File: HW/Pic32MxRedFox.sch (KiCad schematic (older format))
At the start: 40 parts, among them J1 USB_C_Receptacle_USB2.0, J2 Conn_02x05_Odd_Even, J3 Conn_01x20, J4 Conn_01x20, SW1 SW_Push, SW2 SW_Push, U1 LD1117S33TR_SOT223, U2 LN1134A332MR-G, U3 SRV05-4, U4 PIC32MX270F256D-IPT, Y1 Crystal_GND2, Y2 Crystal

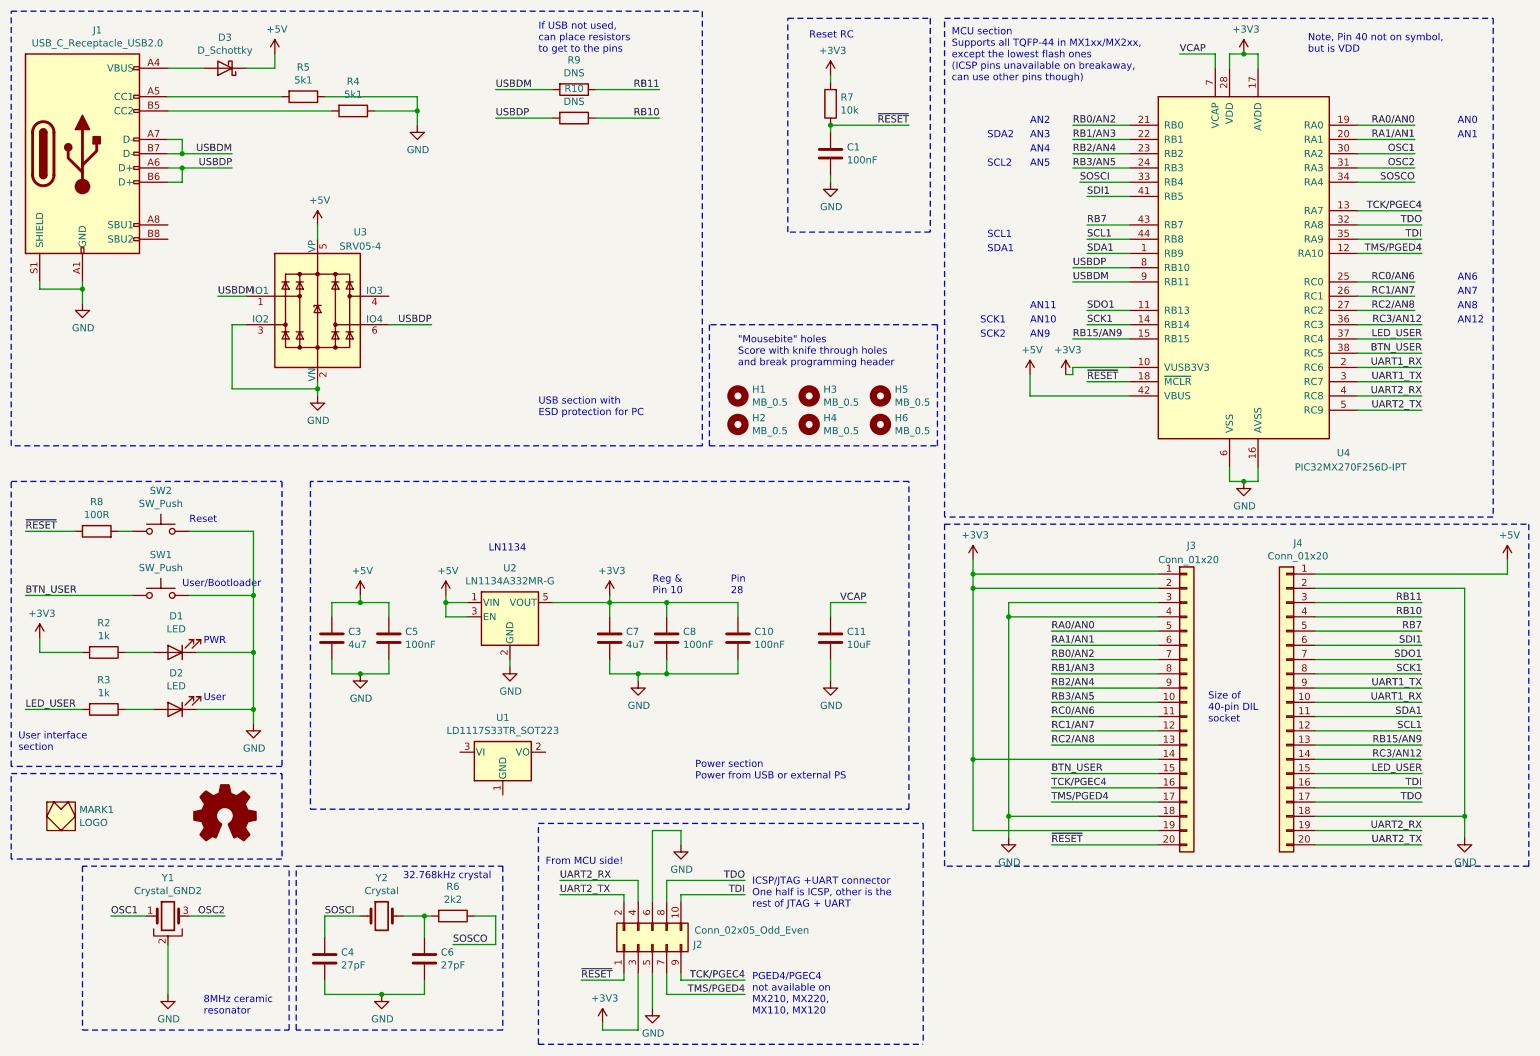
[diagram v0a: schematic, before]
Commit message: New revision that actually fits in a DIP40 socket. Pinout stays the same.
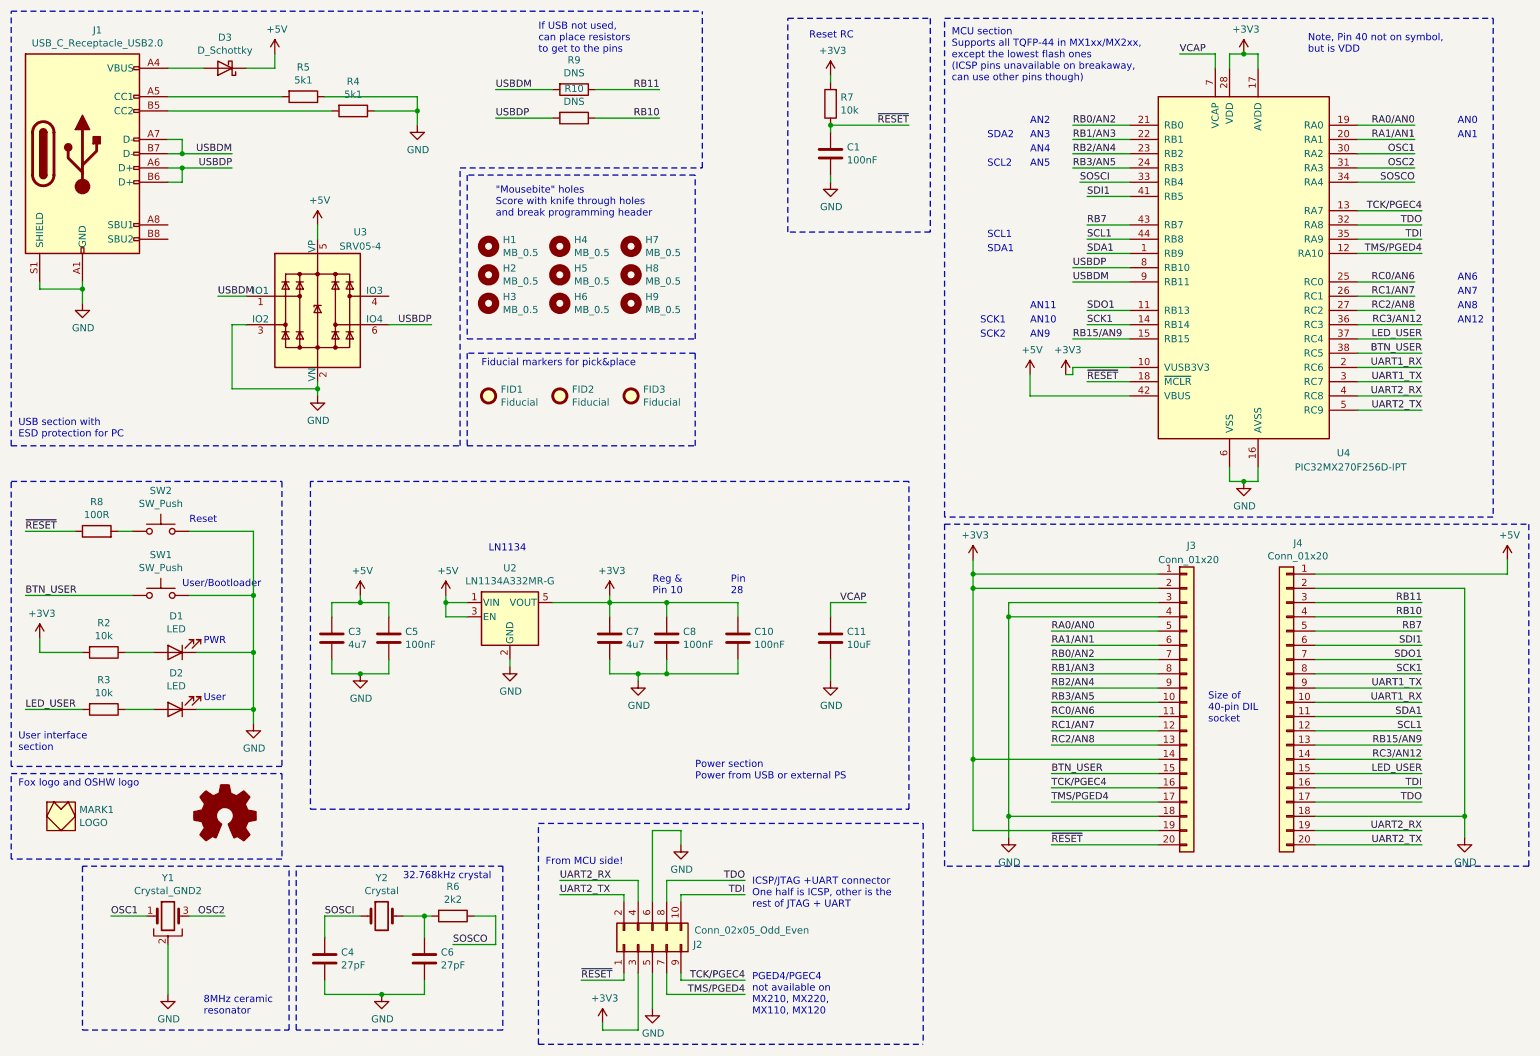
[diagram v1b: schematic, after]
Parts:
- removed U1: LD1117S33TR_SOT223, Package_TO_SOT_SMD:SOT-223-3_TabPin2, symbol Regulator_Linear:LD1117S33TR_SOT223
- added FID1, FID2, FID3: Fiducial, Fiducial:Fiducial_0.5mm_Mask1mm, symbol Mechanical:Fiducial
- added H7, H8, H9: MB_0.5, KiCAD library:MouseBiteHole_0.5mm, symbol Mechanical:MountingHole
- added MARK2: Logo_Open_Hardware_Small, Symbol:OSHW-Logo_5.7x6mm_SilkScreen, symbol Graphic:Logo_Open_Hardware_Small
- R2, R3: value 1k -> 10k
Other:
- note added: "Fiducial markers for pick&place"
- note added: "Fox logo and OSHW logo"
- moved on the sheet: H1, H2, H3, H4, H5, H6
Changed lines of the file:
@@
 P 1150 5000
 F 0 "R2" V 943 5000 50  0000 C CNN
-F 1 "1k" V 1034 5000 50  0000 C CNN
+F 1 "10k" V 1034 5000 50  0000 C CNN
 F 2 "Resistor_SMD:R_0603_1608Metric_Pad1.05x0.95mm_HandSolder" V 1080 5000 50  0001 C CNN
 F 3 "~" H 1150 5000 50  0001 C CNN
@@
 P 1150 5400
 F 0 "R3" V 943 5400 50  0000 C CNN
-F 1 "1k" V 1034 5400 50  0000 C CNN
+F 1 "10k" V 1034 5400 50  0000 C CNN
 F 2 "Resistor_SMD:R_0603_1608Metric_Pad1.05x0.95mm_HandSolder" V 1080 5400 50  0001 C CNN
 F 3 "~" H 1150 5400 50  0001 C CNN
@@
 L Mechanical:MountingHole H1
 U 1 1 5DA5CA50
-P 5600 3200
-F 0 "H1" H 5700 3246 50  0000 L CNN
-F 1 "MB_0.5" H 5700 3155 50  0000 L CNN
-F 2 "KiCAD library:MouseBiteHole_0.5mm" H 5600 3200 50  0001 C CNN
-F 3 "~" H 5600 3200 50  0001 C CNN
-	1    5600 3200
+P 3850 2150
+F 0 "H1" H 3950 2196 50  0000 L CNN
+F 1 "MB_0.5" H 3950 2105 50  0000 L CNN
+F 2 "KiCAD library:MouseBiteHole_0.5mm" H 3850 2150 50  0001 C CNN
+F 3 "~" H 3850 2150 50  0001 C CNN
+	1    3850 2150
 	1    0    0    -1
 $EndComp
@@
 L Mechanical:MountingHole H3
 U 1 1 5DA6CF06
-P 6100 3200
-F 0 "H3" H 6200 3246 50  0000 L CNN
-F 1 "MB_0.5" H 6200 3155 50  0000 L CNN
-F 2 "KiCAD library:MouseBiteHole_0.5mm" H 6100 3200 50  0001 C CNN
-F 3 "~" H 6100 3200 50  0001 C CNN
-	1    6100 3200
+P 3850 2550
+F 0 "H3" H 3950 2596 50  0000 L CNN
+F 1 "MB_0.5" H 3950 2505 50  0000 L CNN
+F 2 "KiCAD library:MouseBiteHole_0.5mm" H 3850 2550 50  0001 C CNN
+F 3 "~" H 3850 2550 50  0001 C CNN
+	1    3850 2550
 	1    0    0    -1
 $EndComp
@@
 L Mechanical:MountingHole H5
 U 1 1 5DA6CF76
-P 6600 3200
-F 0 "H5" H 6700 3246 50  0000 L CNN
-F 1 "MB_0.5" H 6700 3155 50  0000 L CNN
-F 2 "KiCAD library:MouseBiteHole_0.5mm" H 6600 3200 50  0001 C CNN
-F 3 "~" H 6600 3200 50  0001 C CNN
-	1    6600 3200
+P 4350 2350
+F 0 "H5" H 4450 2396 50  0000 L CNN
+F 1 "MB_0.5" H 4450 2305 50  0000 L CNN
+F 2 "KiCAD library:MouseBiteHole_0.5mm" H 4350 2350 50  0001 C CNN
+F 3 "~" H 4350 2350 50  0001 C CNN
+	1    4350 2350
 	1    0    0    -1
 $EndComp
@@
 L Mechanical:MountingHole H2
 U 1 1 5DA6D2CE
-P 5600 3400
-F 0 "H2" H 5700 3446 50  0000 L CNN
-F 1 "MB_0.5" H 5700 3355 50  0000 L CNN
-F 2 "KiCAD library:MouseBiteHole_0.5mm" H 5600 3400 50  0001 C CNN
-F 3 "~" H 5600 3400 50  0001 C CNN
-	1    5600 3400
+P 3850 2350
+F 0 "H2" H 3950 2396 50  0000 L CNN
+F 1 "MB_0.5" H 3950 2305 50  0000 L CNN
+F 2 "KiCAD library:MouseBiteHole_0.5mm" H 3850 2350 50  0001 C CNN
+F 3 "~" H 3850 2350 50  0001 C CNN
+	1    3850 2350
 	1    0    0    -1
 $EndComp
@@
 L Mechanical:MountingHole H4
 U 1 1 5DA7CA40
-P 6100 3400
-F 0 "H4" H 6200 3446 50  0000 L CNN
-F 1 "MB_0.5" H 6200 3355 50  0000 L CNN
-F 2 "KiCAD library:MouseBiteHole_0.5mm" H 6100 3400 50  0001 C CNN
-F 3 "~" H 6100 3400 50  0001 C CNN
-	1    6100 3400
+P 4350 2150
+F 0 "H4" H 4450 2196 50  0000 L CNN
+F 1 "MB_0.5" H 4450 2105 50  0000 L CNN
+F 2 "KiCAD library:MouseBiteHole_0.5mm" H 4350 2150 50  0001 C CNN
+F 3 "~" H 4350 2150 50  0001 C CNN
+	1    4350 2150
 	1    0    0    -1
 $EndComp
@@
 L Mechanical:MountingHole H6
 U 1 1 5DA7CAB4
-P 6600 3400
-F 0 "H6" H 6700 3446 50  0000 L CNN
-F 1 "MB_0.5" H 6700 3355 50  0000 L CNN
-F 2 "KiCAD library:MouseBiteHole_0.5mm" H 6600 3400 50  0001 C CNN
-F 3 "~" H 6600 3400 50  0001 C CNN
-	1    6600 3400
+P 4350 2550
+F 0 "H6" H 4450 2596 50  0000 L CNN
+F 1 "MB_0.5" H 4450 2505 50  0000 L CNN
+F 2 "KiCAD library:MouseBiteHole_0.5mm" H 4350 2550 50  0001 C CNN
+F 3 "~" H 4350 2550 50  0001 C CNN
+	1    4350 2550
 	1    0    0    -1
 $EndComp
@@
 	500  500  5350 500
 Wire Notes Line
-	5350 500  5350 3550
-Wire Notes Line
-	5350 3550 500  3550
-Wire Notes Line
 	500  3550 500  500
-Text Notes 4200 3350 0    50   ~ 0
+Text Notes 550  3500 0    50   ~ 0
 USB section with \nESD protection for PC
 Wire Notes Line
-	5400 3550 7000 3550
-Wire Notes Line
-	7000 3550 7000 2700
-Wire Notes Line
-	7000 2700 5400 2700
-Wire Notes Line
-	5400 2700 5400 3550
-Text Notes 5600 3000 0    50   ~ 0
+	3700 2800 5300 2800
+Wire Notes Line
+	5300 2800 5300 1650
+Wire Notes Line
+	5300 1650 3700 1650
+Wire Notes Line
+	3700 1650 3700 2800
+Text Notes 3900 1950 0    50   ~ 0
 "Mousebite" holes\nScore with knife through holes\nand break programming header
 Wire Notes Line
@@
 	500  6450 500  5850
 $Comp
-L Graphic:Logo_Open_Hardware_Small #LOGO1
+L Graphic:Logo_Open_Hardware_Small MARK2
 U 1 1 5DC4579F
 P 2000 6150
-F 0 "#LOGO1" H 2000 6425 50  0001 C CNN
+F 0 "MARK2" H 2000 6425 50  0001 C CNN
 F 1 "Logo_Open_Hardware_Small" H 2000 5925 50  0001 C CNN
-F 2 "" H 2000 6150 50  0001 C CNN
+F 2 "Symbol:OSHW-Logo_5.7x6mm_SilkScreen" H 2000 6150 50  0001 C CNN
 F 3 "~" H 2000 6150 50  0001 C CNN
 	1    2000 6150
@@
 	5100 5150 5600 5150
 $Comp
-L Regulator_Linear:LD1117S33TR_SOT223 U1
-U 1 1 601472C4
-P 3950 5700
-F 0 "U1" H 3950 5942 50  0000 C CNN
-F 1 "LD1117S33TR_SOT223" H 3950 5851 50  0000 C CNN
-F 2 "Package_TO_SOT_SMD:SOT-223-3_TabPin2" H 3950 5900 50  0001 C CNN
-F 3 "http://www.st.com/st-web-ui/static/active/en/resource/technical/document/datasheet/CD00000544.pdf" H 4050 5450 50  0001 C CNN
-	1    3950 5700
-	1    0    0    -1
-$EndComp
+L Mechanical:MountingHole H8
+U 1 1 600B9C19
+P 4850 2350
+F 0 "H8" H 4950 2396 50  0000 L CNN
+F 1 "MB_0.5" H 4950 2305 50  0000 L CNN
+F 2 "KiCAD library:MouseBiteHole_0.5mm" H 4850 2350 50  0001 C CNN
+F 3 "~" H 4850 2350 50  0001 C CNN
+	1    4850 2350
+	1    0    0    -1
+$EndComp
+$Comp
+L Mechanical:MountingHole H7
+U 1 1 600B9C1F
+P 4850 2150
+F 0 "H7" H 4950 2196 50  0000 L CNN
+F 1 "MB_0.5" H 4950 2105 50  0000 L CNN
+F 2 "KiCAD library:MouseBiteHole_0.5mm" H 4850 2150 50  0001 C CNN
+F 3 "~" H 4850 2150 50  0001 C CNN
+	1    4850 2150
+	1    0    0    -1
+$EndComp
+$Comp
+L Mechanical:MountingHole H9
+U 1 1 600B9C25
+P 4850 2550
+F 0 "H9" H 4950 2596 50  0000 L CNN
+F 1 "MB_0.5" H 4950 2505 50  0000 L CNN
+F 2 "KiCAD library:MouseBiteHole_0.5mm" H 4850 2550 50  0001 C CNN
+F 3 "~" H 4850 2550 50  0001 C CNN
+	1    4850 2550
+	1    0    0    -1
+$EndComp
+Wire Notes Line
+	3650 3550 3650 1600
+Wire Notes Line
+	3650 1600 5350 1600
+Wire Notes Line
+	500  3550 3650 3550
+Wire Notes Line
+	5350 1600 5350 500
+Text Notes 550  5950 0    50   ~ 0
+Fox logo and OSHW logo
+Wire Notes Line
+	3700 2900 3700 3550
+Wire Notes Line
+	3700 3550 5300 3550
+Wire Notes Line
+	5300 3550 5300 2900
+Wire Notes Line
+	5300 2900 3700 2900
+$Comp
+L Mechanical:Fiducial FID1
+U 1 1 601A3451
+P 3850 3200
+F 0 "FID1" H 3935 3246 50  0000 L CNN
+F 1 "Fiducial" H 3935 3155 50  0000 L CNN
+F 2 "Fiducial:Fiducial_0.5mm_Mask1mm" H 3850 3200 50  0001 C CNN
+F 3 "~" H 3850 3200 50  0001 C CNN
+	1    3850 3200
+	1    0    0    -1
+$EndComp
+$Comp
+L Mechanical:Fiducial FID2
+U 1 1 601A3850
+P 4350 3200
+F 0 "FID2" H 4435 3246 50  0000 L CNN
+F 1 "Fiducial" H 4435 3155 50  0000 L CNN
+F 2 "Fiducial:Fiducial_0.5mm_Mask1mm" H 4350 3200 50  0001 C CNN
+F 3 "~" H 4350 3200 50  0001 C CNN
+	1    4350 3200
+	1    0    0    -1
+$EndComp
+$Comp
+L Mechanical:Fiducial FID3
+U 1 1 601A3BE7
+P 4850 3200
+F 0 "FID3" H 4935 3246 50  0000 L CNN
+F 1 "Fiducial" H 4935 3155 50  0000 L CNN
+F 2 "Fiducial:Fiducial_0.5mm_Mask1mm" H 4850 3200 50  0001 C CNN
+F 3 "~" H 4850 3200 50  0001 C CNN
+	1    4850 3200
+	1    0    0    -1
+$EndComp
+Text Notes 3800 3000 0    50   ~ 0
+Fiducial markers for pick&place
 $EndSCHEMATC
